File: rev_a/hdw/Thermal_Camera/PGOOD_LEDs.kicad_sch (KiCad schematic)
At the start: 29 parts, among them U2703 74LVC1G97, U2707 74LVC1G97

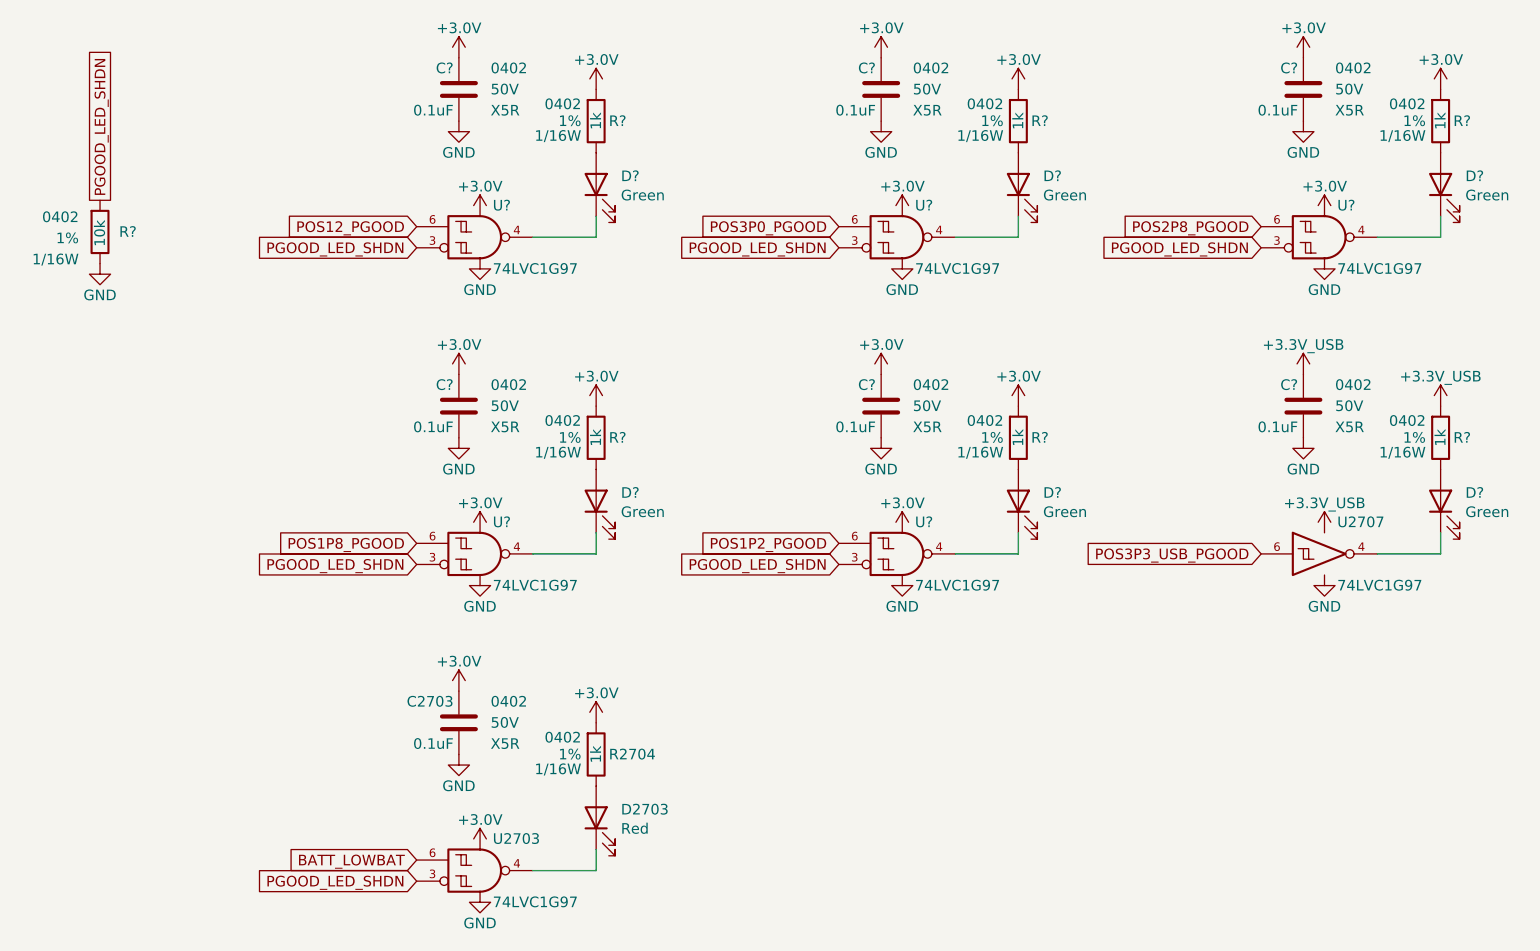
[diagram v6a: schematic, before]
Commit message: got unconnects near zero
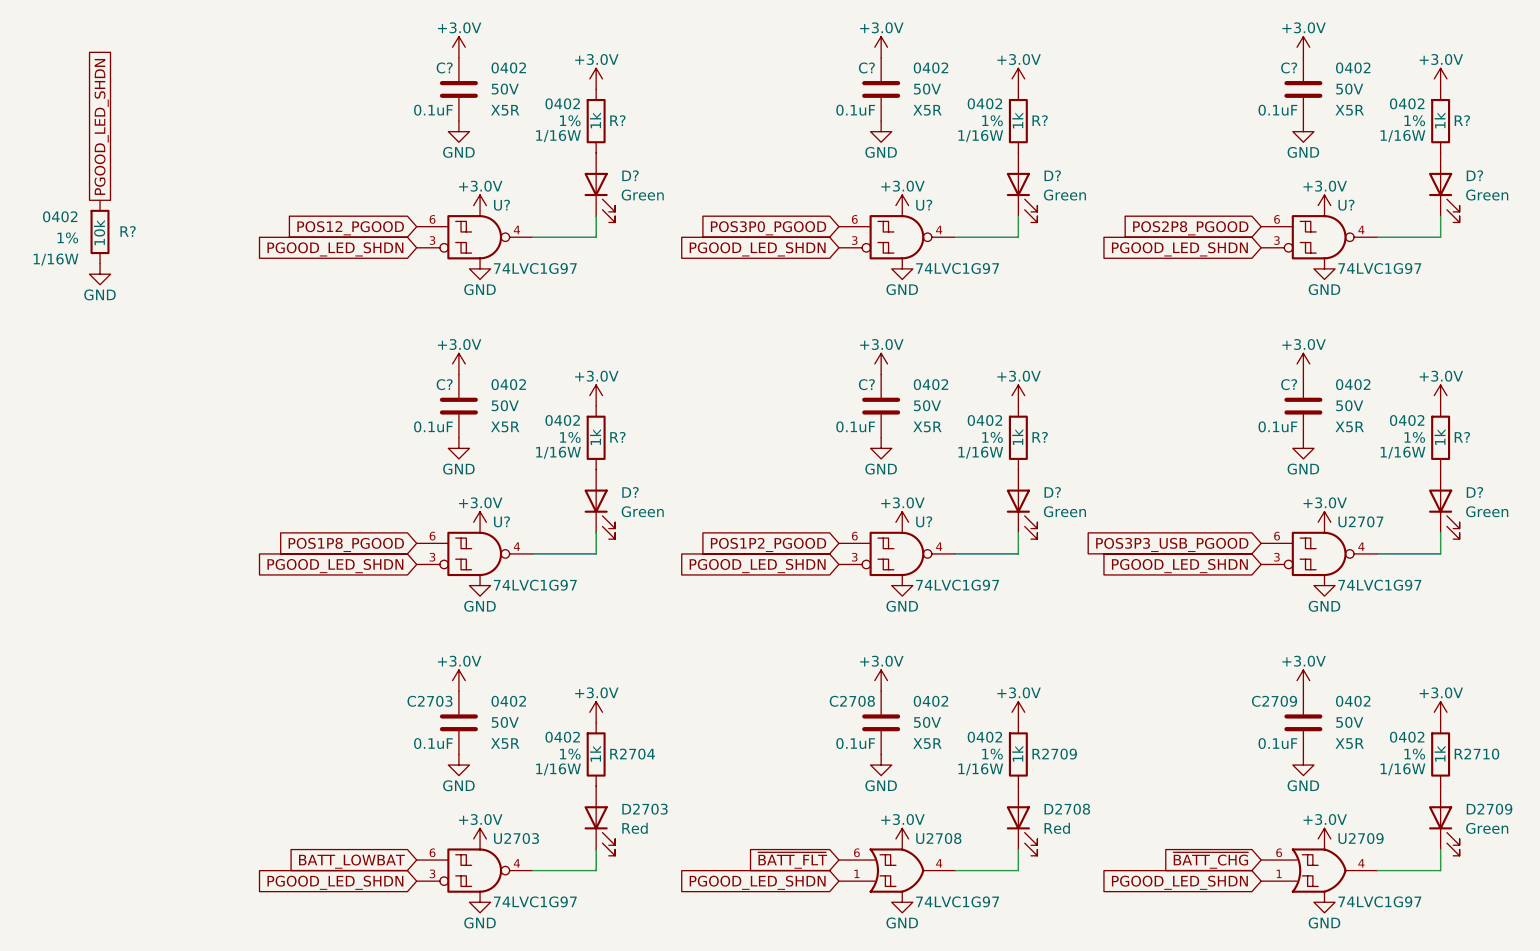
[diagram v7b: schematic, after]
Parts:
- removed U2707: 74LVC1G97, Package_TO_SOT_SMD:SOT-363_SC-70-6, symbol Custom Library:74LVC1G97_Power_NOT
- added C2708, C2709: 0.1uF, Capacitors_SMD:C_0402, symbol Custom_Library:C_Custom
- added D2708: Red, LEDs:LED_0402, symbol Device:LED
- added D2709: Green, LEDs:LED_0402, symbol Device:LED
- added R2709, R2710: 1k, Resistors_SMD:R_0402, symbol Custom_Library:R_Custom
- added U2707: 74LVC1G97, Package_TO_SOT_SMD:SOT-363_SC-70-6, symbol Custom_Library:74LVC1G97_Power_NAND_INV
- added U2708, U2709: 74LVC1G97, Package_TO_SOT_SMD:SOT-363_SC-70-6, symbol Custom Library:74LVC1G97_Power_OR
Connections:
- net +3.3V_USB is gone; now on net +3.0V: C?.1, R?.1
- net +3.0V: now also C2708.1, C2709.1, R2709.1, R2710.1, U2707.1 (VCC), U2707.5 (VCC), U2708.3 (VCC), U2708.5 (VCC), U2709.3 (VCC), U2709.5 (VCC)
- net GND: now also C2708.2, C2709.2, U2707.2 (GND), U2708.2 (GND), U2709.2 (GND)
- net PGOOD_LED_SHDN: now also U2707.3, U2708.1, U2709.1
- net POS3P3_USB_PGOOD: now also U2707.6
- net at D?.1 (K): now also U2707.4
- new net: D2708.1 (K), U2708.4
- new net: D2708.2 (A), R2709.2
- new net: D2709.1 (K), U2709.4
- new net: D2709.2 (A), R2710.2
- new net ~{BATT_CHG}: U2709.6
- new net ~{BATT_FLT}: U2708.6
